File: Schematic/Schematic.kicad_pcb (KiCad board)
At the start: 2 copper layers, 33 x 45.7 mm, 2 parts, among them U1 NRF52840-DONGLE

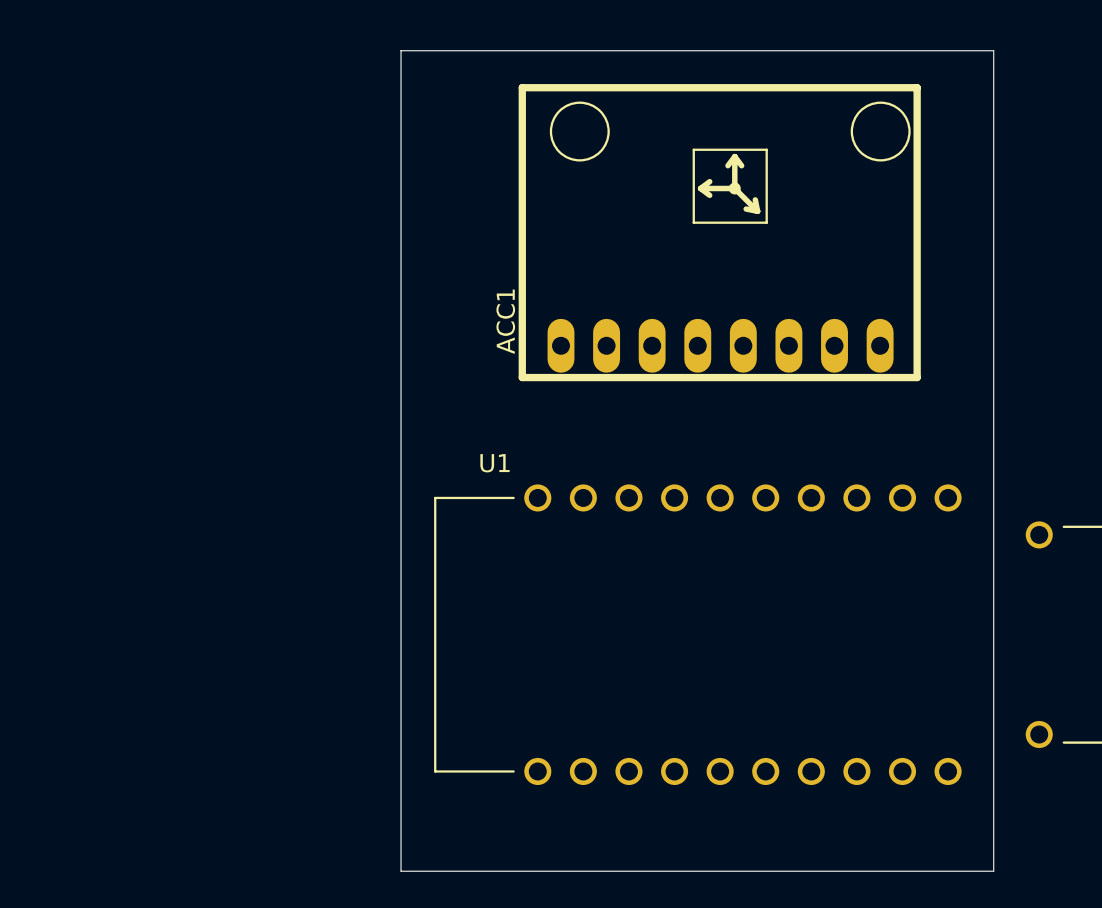
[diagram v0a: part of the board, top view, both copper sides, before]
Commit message: PCB: adding the required symbols, footprints and 3D models
- create generic paths to the symbos and footprints, so there is no problem with setup on the other machine
- adding further PCB elements of the project
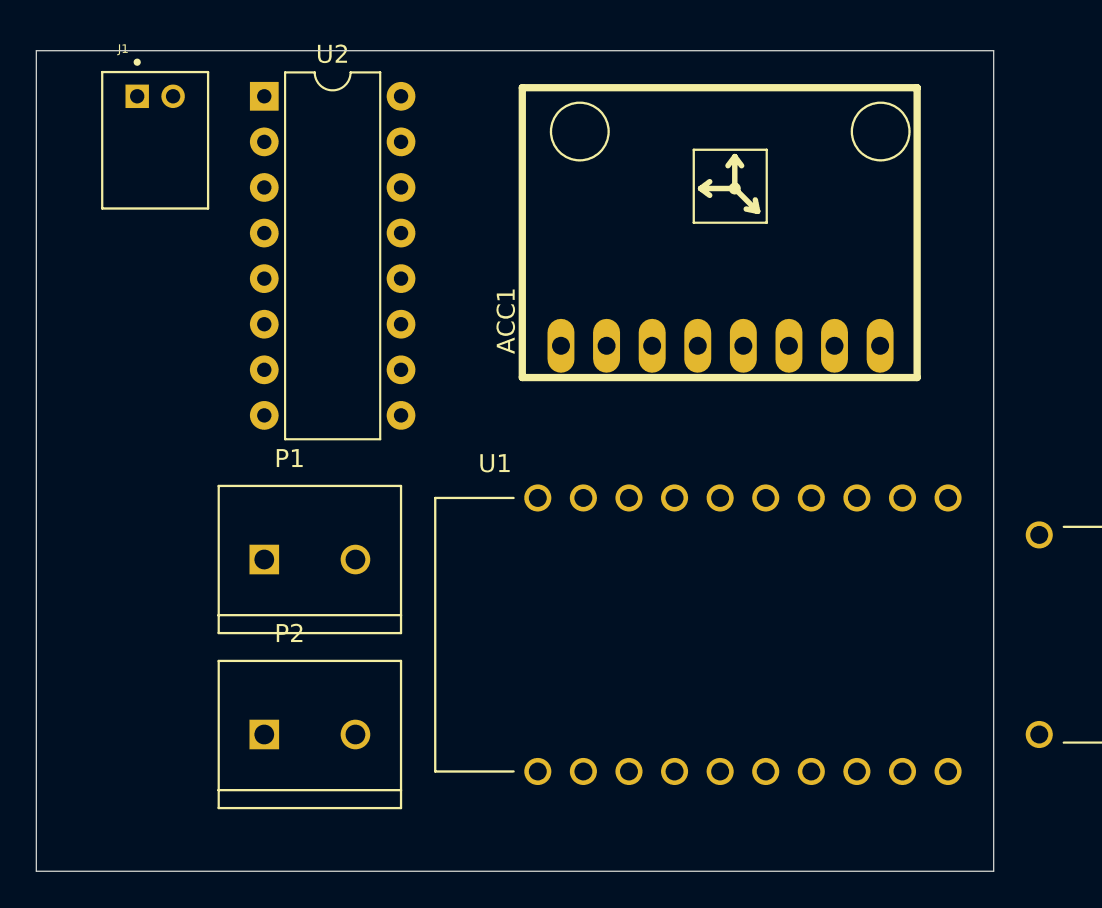
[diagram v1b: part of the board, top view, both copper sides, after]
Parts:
- added J1: S2B-PH-K-S_LF__SN_, S2B-PH-K-S_LF__SN_:JST_S2B-PH-K-S_LF__SN_, F.Cu at (110.8, 66.0)
- added P1: 282837-2, 282837-2:TE_282837-2, F.Cu at (119.4, 91.8)
- added P2: 282837-2, 282837-2:TE_282837-2, F.Cu at (119.4, 101.6)
- added U2: L293D, Package_DIP:DIP-16_W7.62mm, F.Cu at (116.8, 66.0)
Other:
- board size 33 x 45.7 mm -> 53.3 x 45.7 mm

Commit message: PCB: Added all neecesseary symbols, footprints and 3d models
-create an demo PCB
-create 3dvis folder with apperance of the boards
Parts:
- added C1: 100uF, Capacitor_THT:C_Disc_D7.5mm_W4.4mm_P5.00mm, F.Cu at (175.3, 116.8)
- added C2: 100uF, Capacitor_THT:C_Disc_D7.5mm_W4.4mm_P5.00mm, F.Cu at (149.9, 116.8)
- added C3: 100uF, Capacitor_THT:C_Disc_D7.5mm_W4.4mm_P5.00mm, F.Cu at (149.9, 122.8)
- added R1: 100R, Resistor_THT:R_Axial_DIN0207_L6.3mm_D2.5mm_P5.08mm_Vertical, F.Cu at (162.6, 124.5)
- added R2: 100R, Resistor_THT:R_Axial_DIN0207_L6.3mm_D2.5mm_P5.08mm_Vertical, F.Cu at (162.6, 115.3)
- added R3: 100R, Resistor_THT:R_Axial_DIN0207_L6.3mm_D2.5mm_P5.08mm_Vertical, F.Cu at (162.6, 119.4)
- added S1: 1101M2S3CQE2, 1101M2S3CQE2:SW_1101M2S3CQE2, F.Cu at (178.2, 127.0)
- added U3: LM1117DT-3.3, Package_TO_SOT_SMD:TO-252-3_TabPin2, F.Cu at (192.6, 117.9)
- added U4: YAAJ_DCDC_StepDown_LM2596, lm256:YAAJ_DCDC_StepDown_LM2596, F.Cu at (149.9, 88.9)
- J1: moved to B.Cu
- moved ACC1 81.6 mm to (232.0, 103.3)
- moved U1 81.6 mm to (228.1, 117.6)
- moved U2 81.6 mm to (195.6, 87.6)
- moved J1 42.0 mm to (128.5, 104.1), turned to 180 degrees
- moved P1 32.6 mm to (132.1, 121.9)
- moved P2 16.3 mm to (132.1, 91.4)
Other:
- board size 53.3 x 45.7 mm -> 116.8 x 45.7 mm

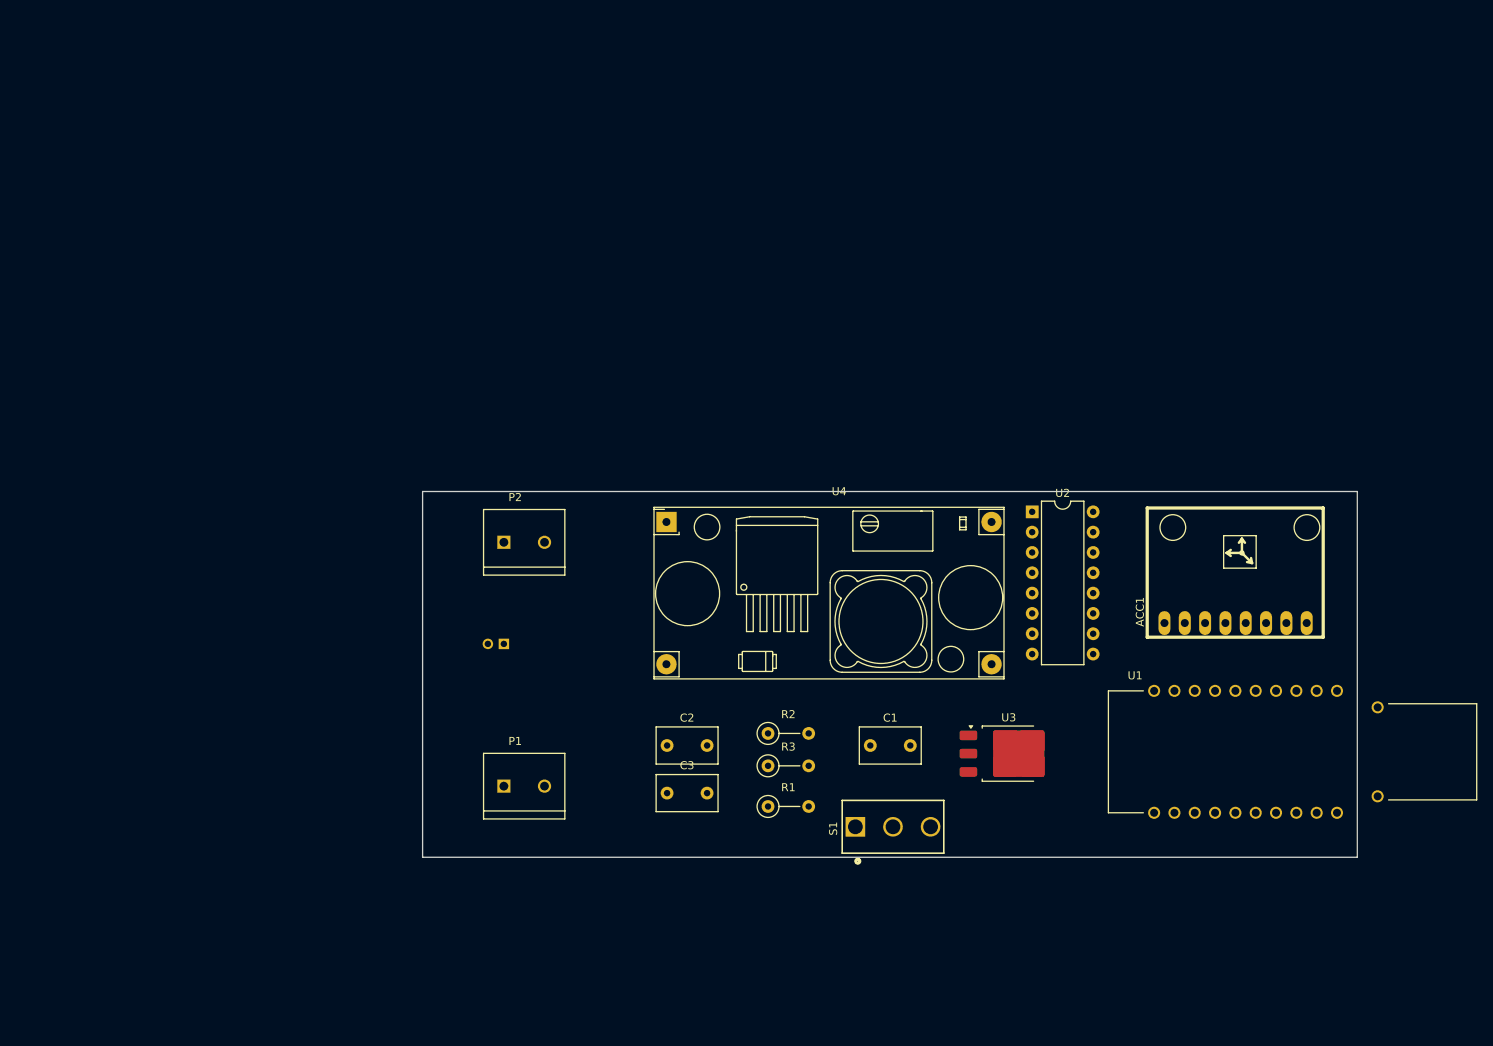
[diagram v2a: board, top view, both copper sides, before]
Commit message: PCB: completing the electrical diagram
-fix with the H bridge (we have to use TB6612FNG which can operate at PWM 3.3 V
-complete schematic
-create prototype PCB schematic
-track PCB paths
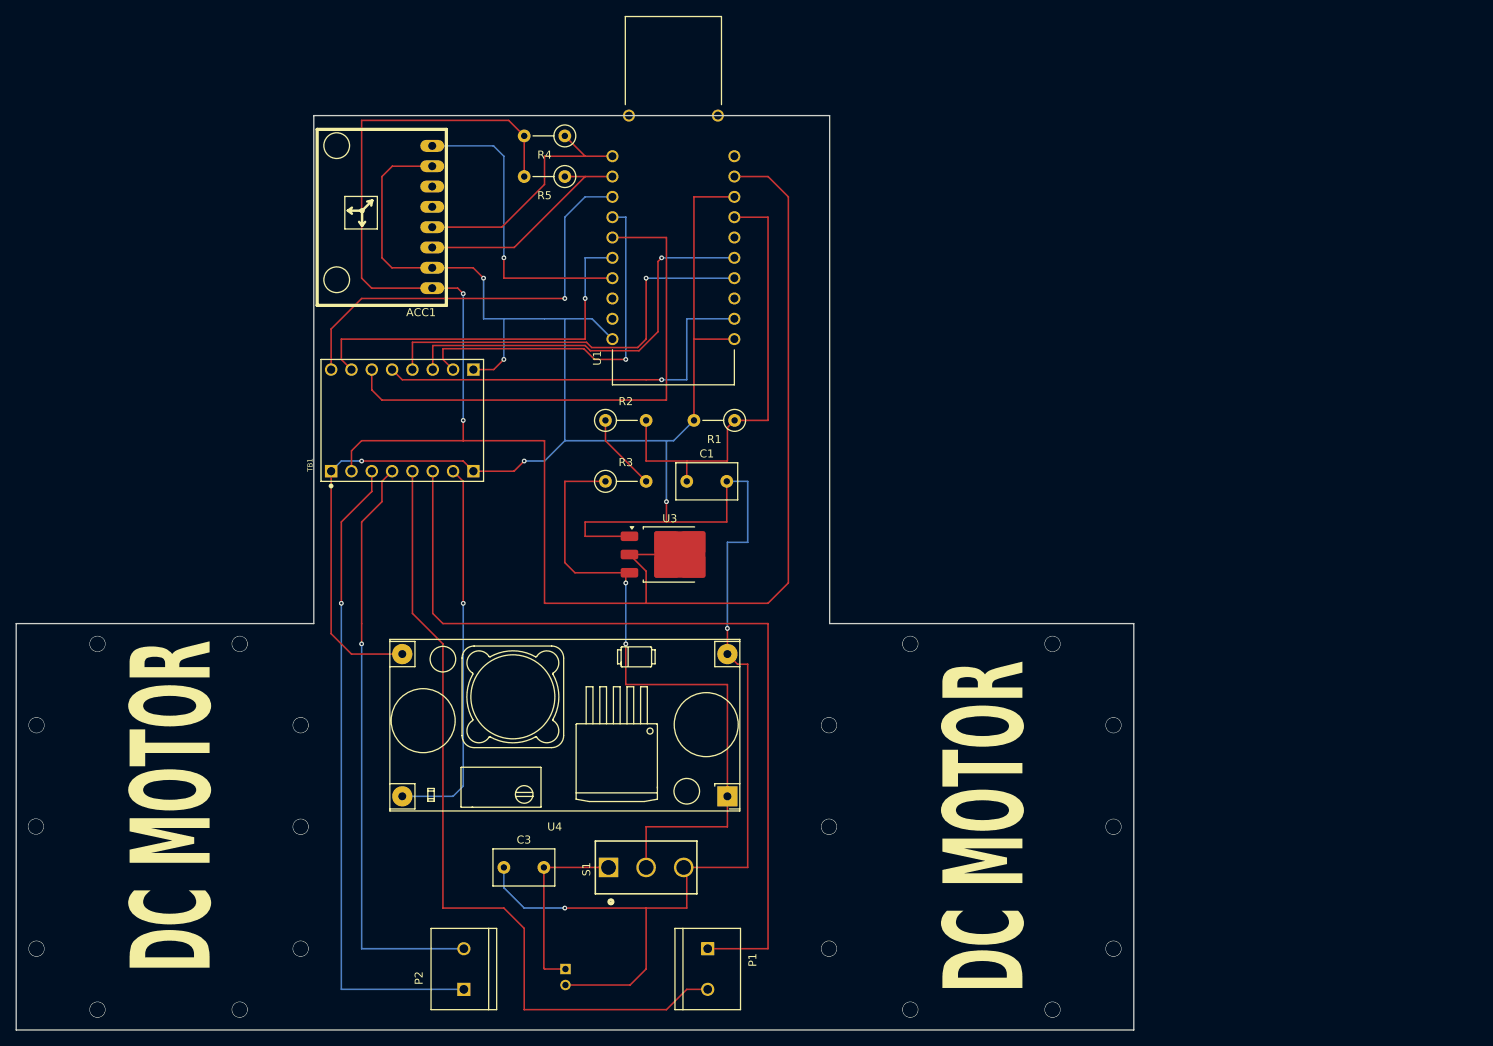
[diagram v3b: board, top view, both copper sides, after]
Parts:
- removed C2: 100uF, Capacitor_THT:C_Disc_D7.5mm_W4.4mm_P5.00mm
- removed U2: L293D, Package_DIP:DIP-16_W7.62mm
- added R4: 10kR, Resistor_THT:R_Axial_DIN0207_L6.3mm_D2.5mm_P5.08mm_Vertical, F.Cu at (137.2, 40.6)
- added R5: 10kR, Resistor_THT:R_Axial_DIN0207_L6.3mm_D2.5mm_P5.08mm_Vertical, F.Cu at (137.2, 45.7)
- added TB1: POLOLU-713, POLOLU-713:SHIELD_POLOLU-713, F.Cu at (116.8, 76.2)
- R1, R2, R3: value 100R -> 100k
- moved ACC1 126.7 mm to (122.4, 39.8), turned to 180 degrees
- moved U1 103.6 mm to (150.7, 48.7), turned to 90 degrees
- moved P2 53.9 mm to (124.5, 144.8), turned to 90 degrees
- moved U3 49.1 mm to (150.3, 93.0)
- moved R1 48.4 mm to (158.4, 76.2), turned to 180 degrees
- moved R2 44.1 mm to (142.2, 76.2)
- moved J1 42.5 mm to (137.2, 145.8), turned to -90 degrees
- moved R3 41.0 mm to (142.2, 83.8)
- moved C1 40.2 mm to (152.4, 83.8)
- moved U4 35.1 mm to (157.5, 123.2), turned to 180 degrees
- moved P1 32.4 mm to (155.0, 144.8), turned to -90 degrees
- moved S1 31.3 mm to (147.3, 132.1)
- moved C3 22.4 mm to (129.5, 132.1)
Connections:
- ACC1 pad AD0: unconnected-(ACC1-PadAD0) -> GND
- ACC1 pad GND: unconnected-(ACC1-PadGND) -> GND
- ACC1 pad INT: unconnected-(ACC1-PadINT) -> IMU_INT
- ACC1 pad SCL: unconnected-(ACC1-PadSCL) -> SCL
- ACC1 pad SDA: unconnected-(ACC1-PadSDA) -> SDA
- ACC1 pad VCC: unconnected-(ACC1-PadVCC) -> 3_3V
- C1 pad 1: unconnected-(C1-Pad1) -> ADC_BAT
- C1 pad 2: unconnected-(C1-Pad2) -> GND
- C3 pad 1: unconnected-(C3-Pad1) -> GND
- C3 pad 2: unconnected-(C3-Pad2) -> VDD
- J1 pad 1: unconnected-(J1-Pad1) -> VDD
- J1 pad 2: unconnected-(J1-Pad2) -> GND
- P1 pad 1: unconnected-(P1-Pad1) -> B01
- P1 pad 2: unconnected-(P1-Pad2) -> B02
- P2 pad 1: unconnected-(P2-Pad1) -> A01
- P2 pad 2: unconnected-(P2-Pad2) -> A02
- R1 pad 1: unconnected-(R1-Pad1) -> ADC_BAT
- R1 pad 2: unconnected-(R1-Pad2) -> GND
- R2 pad 1: unconnected-(R2-Pad1) -> Net-(R2-Pad1)
- R2 pad 2: unconnected-(R2-Pad2) -> ADC_BAT
- R3 pad 1: unconnected-(R3-Pad1) -> VDD_bat
- R3 pad 2: unconnected-(R3-Pad2) -> Net-(R2-Pad1)
- S1 pad 1: unconnected-(S1-Pad1) -> VDD
- S1 pad 2: unconnected-(S1-Pad2) -> VDD_bat
- S1 pad 3: unconnected-(S1-Pad3) -> GND
- U1 pad 0.02: unconnected-(U1-Pad0.02) -> B2_IN
- U1 pad 0.13: unconnected-(U1-Pad0.13) -> SDA
- U1 pad 0.15: unconnected-(U1-Pad0.15) -> SCL
- U1 pad 0.17: unconnected-(U1-Pad0.17) -> PWM_A
- U1 pad 0.20: unconnected-(U1-Pad0.20) -> PWM_B
- U1 pad 0.22: unconnected-(U1-Pad0.22) -> A1_IN
- U1 pad 0.24: unconnected-(U1-Pad0.24) -> A2_IN
- U1 pad 0.31: unconnected-(U1-Pad0.31) -> ADC_BAT
- U1 pad 1.00: unconnected-(U1-Pad1.00) -> IMU_INT
- U1 pad 1.10: unconnected-(U1-Pad1.10) -> H_DRIVE_EN
- U1 pad 1.15: unconnected-(U1-Pad1.15) -> B1_IN
- U1 pad G1: Net-(U1-GND-PadG1) -> GND
- U1 pad G2: Net-(U1-GND-PadG1) -> GND
- U1 pad G3: Net-(U1-GND-PadG1) -> GND
- U1 pad OUT: unconnected-(U1-PadOUT) -> 3_3V
- U3 pad 1: unconnected-(U3-GND-Pad1) -> GND
- U3 pad 2: unconnected-(U3-VO-Pad2) -> 3_3V
- U3 pad 3: unconnected-(U3-VI-Pad3) -> VDD_bat
- U4 pad 1: unconnected-(U4-Vin-Pad1) -> VDD_bat
- U4 pad 2: unconnected-(U4-GND-Pad2) -> GND
- U4 pad 3: unconnected-(U4-GND-Pad3) -> GND
- U4 pad 4: unconnected-(U4-Vout-Pad4) -> 6V
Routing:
- net GND: track 0.00 -> 348.7 mm, vias 0 -> 7
- net 3_3V: track 0.00 -> 226.2 mm, vias 0 -> 2
- net B01: track 0.00 -> 108.4 mm
- net B02: track 0.00 -> 101.6 mm
- net VDD_bat: track 0.00 -> 83.7 mm, vias 0 -> 2
- net A01: track 0.00 -> 81.7 mm, vias 0 -> 1
- net A02: track 0.00 -> 74.0 mm, vias 0 -> 1
- net A1_IN: track 0.00 -> 67.0 mm
- net ADC_BAT: track 0.00 -> 57.0 mm
- net PWM_A: track 0.00 -> 53.0 mm, vias 0 -> 1
- net B1_IN: track 0.00 -> 52.0 mm, vias 0 -> 1
- net B2_IN: track 0.00 -> 50.9 mm, vias 0 -> 1
- net H_DRIVE_EN: track 0.00 -> 50.9 mm, vias 0 -> 1
- net A2_IN: track 0.00 -> 48.4 mm, vias 0 -> 1
- net 6V: track 0.00 -> 48.0 mm, vias 0 -> 1
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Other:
- board size 116.8 x 45.7 mm -> 139.7 x 114.3 mm
- board text added: "DC MOTOR"
